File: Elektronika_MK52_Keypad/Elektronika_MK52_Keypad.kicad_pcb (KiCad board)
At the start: 2 copper layers, 33 parts, among them J1 Keypad PCB, SW1 F, SW10 ШГ←, SW11 Х←П, SW12 4, SW13 5, SW14 6, SW15 +, SW16 *, SW17 ↓↑, SW18 B/O, SW19 БП, SW2 ШГ→, SW20 1, SW21 2, SW22 3, SW23 ↔, SW24 В↑, SW25 A↑, SW26 С/П, SW27 ПП, SW28 0, SW29 ., SW3 П→Х, SW30 /-/, SW31 ВП, SW32 СХ, SW4 7, SW5 8, SW6 9, SW7 -, SW8 ÷, SW9 K

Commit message: Adjusted PCB thickness 1.6mm -> 1.0mm
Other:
- board outline added: 104 x 52.5 mm
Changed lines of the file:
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@@
 	(generator_version "9.0")
 	(general
-		(thickness 1.6)
+		(thickness 1)
 		(legacy_teardrops no)
 	)
@@
 	)
 	(setup
+		(stackup
+			(layer "F.SilkS"
+				(type "Top Silk Screen")
+			)
+			(layer "F.Paste"
+				(type "Top Solder Paste")
+			)
+			(layer "F.Mask"
+				(type "Top Solder Mask")
+				(thickness 0.01)
+			)
+			(layer "F.Cu"
+				(type "copper")
+				(thickness 0.035)
+			)
+			(layer "dielectric 1"
+				(type "core")
+				(thickness 0.91)
+				(material "FR4")
+				(epsilon_r 4.5)
+				(loss_tangent 0.02)
+			)
+			(layer "B.Cu"
+				(type "copper")
+				(thickness 0.035)
+			)
+			(layer "B.Mask"
+				(type "Bottom Solder Mask")
+				(thickness 0.01)
+			)
+			(layer "B.Paste"
+				(type "Bottom Solder Paste")
+			)
+			(layer "B.SilkS"
+				(type "Bottom Silk Screen")
+			)
+			(copper_finish "None")
+			(dielectric_constraints no)
+		)
 		(pad_to_mask_clearance 0)
 		(allow_soldermask_bridges_in_footprints no)
@@
 		(layer "Dwgs.User")
 	)
+	(gr_rect
+		(start 67 44)
+		(end 171 96.5)
+		(stroke
+			(width 0.05)
+			(type default)
+		)
+		(fill no)
+		(layer "Edge.Cuts")
+	)
 	(gr_text "WORK IN PROGRESS"

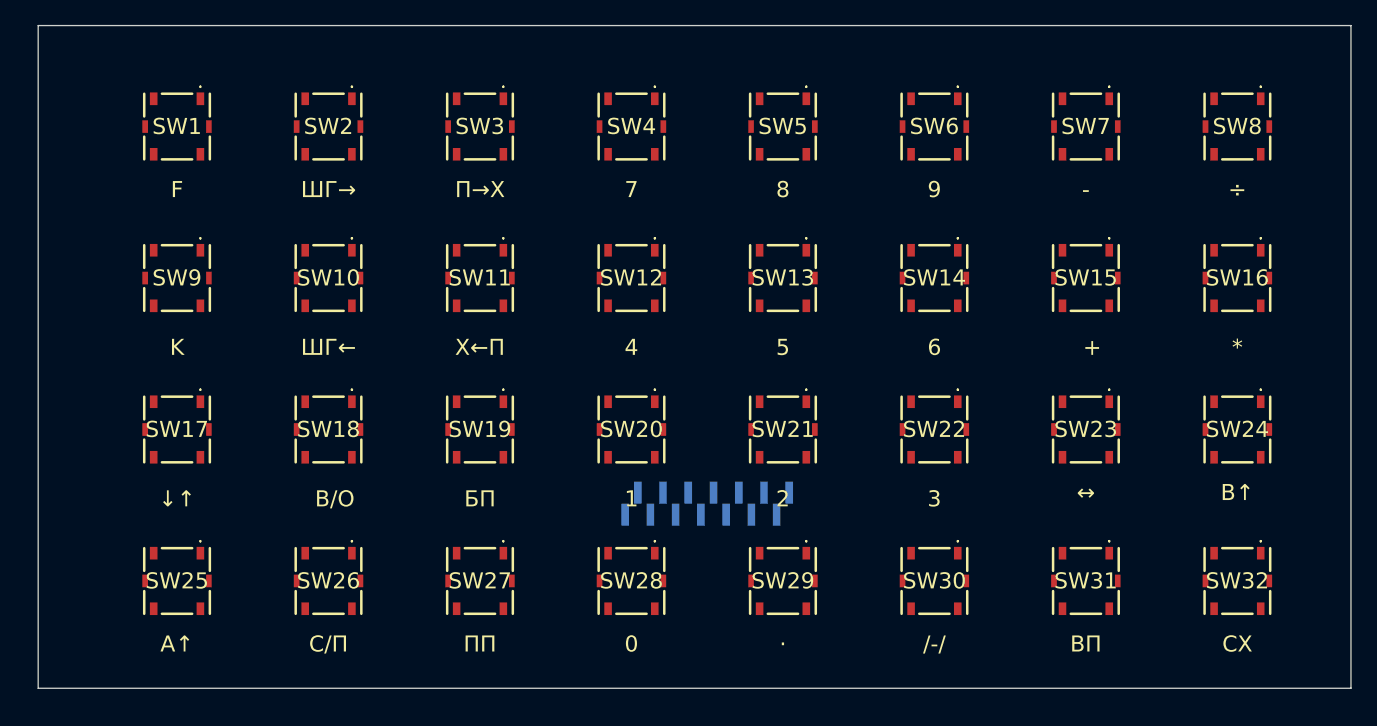
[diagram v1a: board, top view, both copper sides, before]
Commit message: Created PCB outline
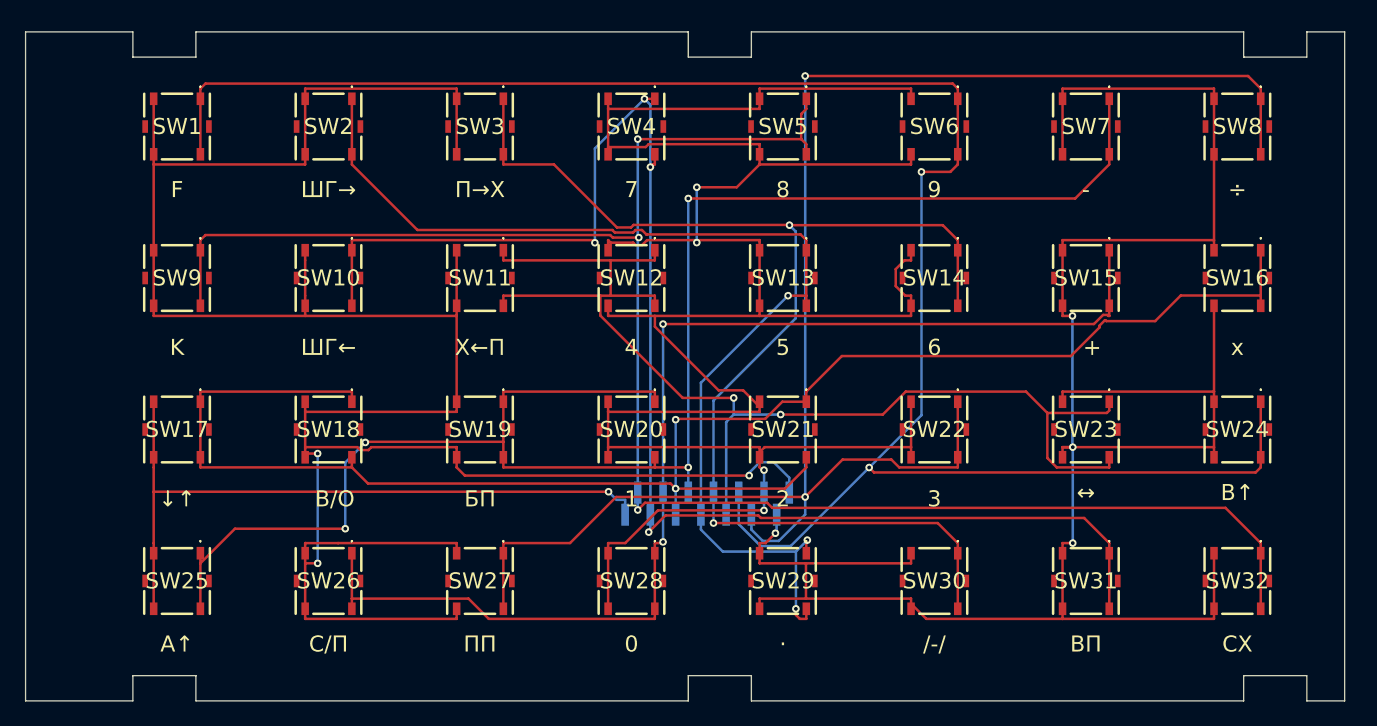
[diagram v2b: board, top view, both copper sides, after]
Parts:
- SW16: value * -> x
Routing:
- net /ROW 1: track 0.00 -> 199.7 mm, vias 0 -> 4
- net /ROW 0: track 0.00 -> 195.8 mm, vias 0 -> 3
- net /ROW 2: track 0.00 -> 175.6 mm, vias 0 -> 4
- net /COL 0: track 0.00 -> 152.5 mm, vias 0 -> 2
- net /COL 3: track 0.00 -> 143.4 mm, vias 0 -> 3
- net /COL 6: track 0.00 -> 132.7 mm, vias 0 -> 2
- net /COL 7: track 0.00 -> 132.7 mm, vias 0 -> 4
- net /COL 8: track 0.00 -> 132.5 mm, vias 0 -> 2
- net /COL 4: track 0.00 -> 117.3 mm, vias 0 -> 4
- net /COL 2: track 0.00 -> 100.8 mm, vias 0 -> 2
- net /COL 5: track 0.00 -> 95.9 mm, vias 0 -> 2
- net /COL 9: track 0.00 -> 93.9 mm, vias 0 -> 2
- net /COL 1: track 0.00 -> 89.3 mm, vias 0 -> 3
- net /ROW 3: track 0.00 -> 55.2 mm, vias 0 -> 1
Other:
- board size 104 x 52.5 mm -> 104.5 x 53 mm

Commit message: initial PCB routing
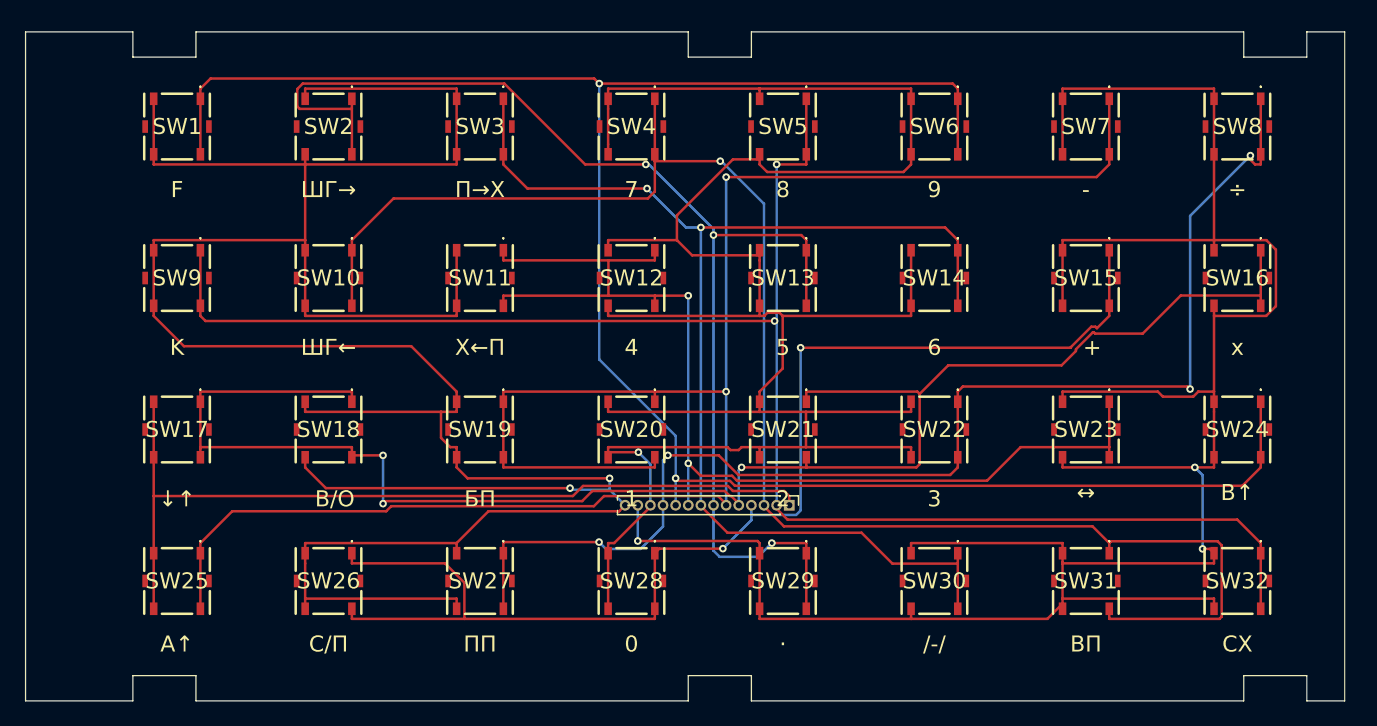
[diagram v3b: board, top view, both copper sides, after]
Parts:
- J1: footprint Connector_PinHeader_1.00mm:PinHeader_1x14_P1.00mm_Vertical_SMD_Pin1Right -> Connector_PinHeader_1.00mm:PinHeader_1x14_P1.00mm_Vertical; moved to F.Cu
- moved J1 6.50 mm to (126.5, 82.0)
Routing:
- net /ROW 0: track 195.8 -> 228.3 mm, vias 3 -> 2
- net /COL 8: track 132.5 -> 100.1 mm, vias 2 -> 4
- net /ROW 2: track 175.6 -> 196.1 mm, vias 4 -> 3
- net /COL 7: track 132.7 -> 148.0 mm, vias 4 -> 2
- net /ROW 3: track 55.2 -> 68.1 mm, vias 1 -> 0
- net /COL 3: track 143.4 -> 130.5 mm, vias 3 -> 2
- net /ROW 1: track 199.7 -> 188.6 mm, vias 4 -> 1
- net /COL 1: track 89.3 -> 99.5 mm
- net /COL 4: track 117.3 -> 126.1 mm, vias 4 -> 1
- net /COL 5: track 95.9 -> 88.7 mm
- net /COL 9: track 93.9 -> 100.9 mm
- net /COL 0: track 152.5 -> 159.4 mm
- net /COL 2: track 100.8 -> 97.6 mm
- net /COL 6: track 132.7 -> 134.6 mm, vias 2 -> 3

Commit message: Adjusted PCB dimensions (thanks Alex!)
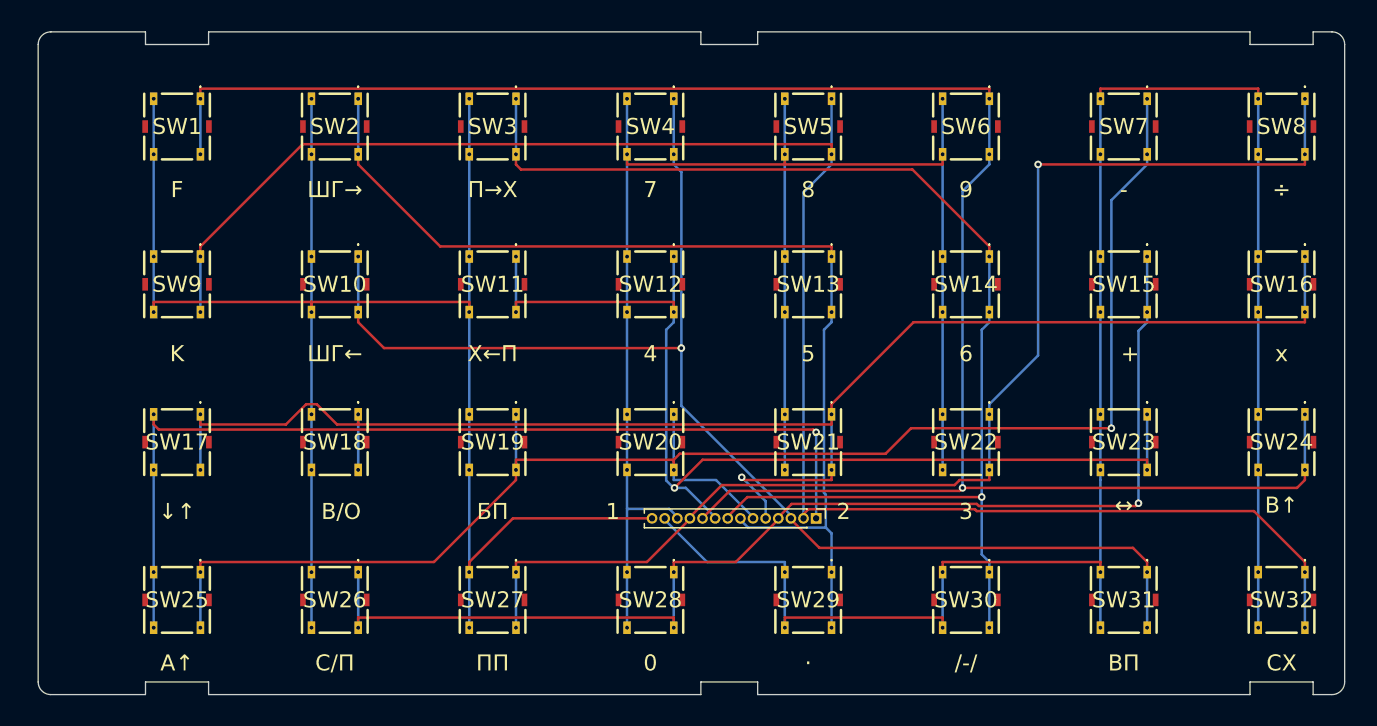
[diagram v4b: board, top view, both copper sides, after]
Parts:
- moved SW32 3.81 mm to (165.5, 89.5)
- moved SW24 3.64 mm to (165.5, 77.0)
- moved SW16 3.54 mm to (165.5, 64.5)
- moved SW8 3.50 mm to (165.5, 52.0)
- moved SW31 3.35 mm to (153.0, 89.5)
- moved SW23 3.16 mm to (153.0, 77.0)
- moved SW15 3.04 mm to (153.0, 64.5)
- moved SW7 3.00 mm to (153.0, 52.0)
- moved SW30 2.92 mm to (140.5, 89.5)
- moved SW22 2.69 mm to (140.5, 77.0)
- moved SW14 2.55 mm to (140.5, 64.5)
- moved SW29 2.50 mm to (128.0, 89.5)
- moved SW6 2.50 mm to (140.5, 52.0)
- moved J1 2.37 mm to (128.6, 83.0)
- moved SW21 2.24 mm to (128.0, 77.0)
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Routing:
- net /ROW 0: track 228.3 -> 144.8 mm, vias 2 -> 0
- net /ROW 1: track 188.6 -> 132.5 mm, vias 1 -> 0
- net /ROW 2: track 196.1 -> 146.7 mm, vias 3 -> 0
- net /COL 4: track 126.1 -> 103.6 mm
- net /COL 7: track 148.0 -> 128.0 mm, vias 2 -> 1
- net /COL 1: track 99.5 -> 83.2 mm, vias 3 -> 0
- net /COL 3: track 130.5 -> 140.7 mm, vias 2 -> 0
- net /COL 6: track 134.6 -> 125.2 mm, vias 3 -> 1
- net /ROW 3: track 68.1 -> 77.3 mm, vias 0 -> 1
- net /COL 9: track 100.9 -> 95.0 mm, vias 2 -> 1
- net /COL 0: track 159.4 -> 154.4 mm, vias 2 -> 1
- net /COL 5: track 88.7 -> 85.2 mm, vias 2 -> 1
- net /COL 8: track 100.1 -> 98.4 mm, vias 4 -> 1
- net /COL 2: track 97.6 -> 97.0 mm, vias 2 -> 1
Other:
- board size 104.5 x 53 mm -> 103.5 x 52.5 mm

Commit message: Revised PCB layout
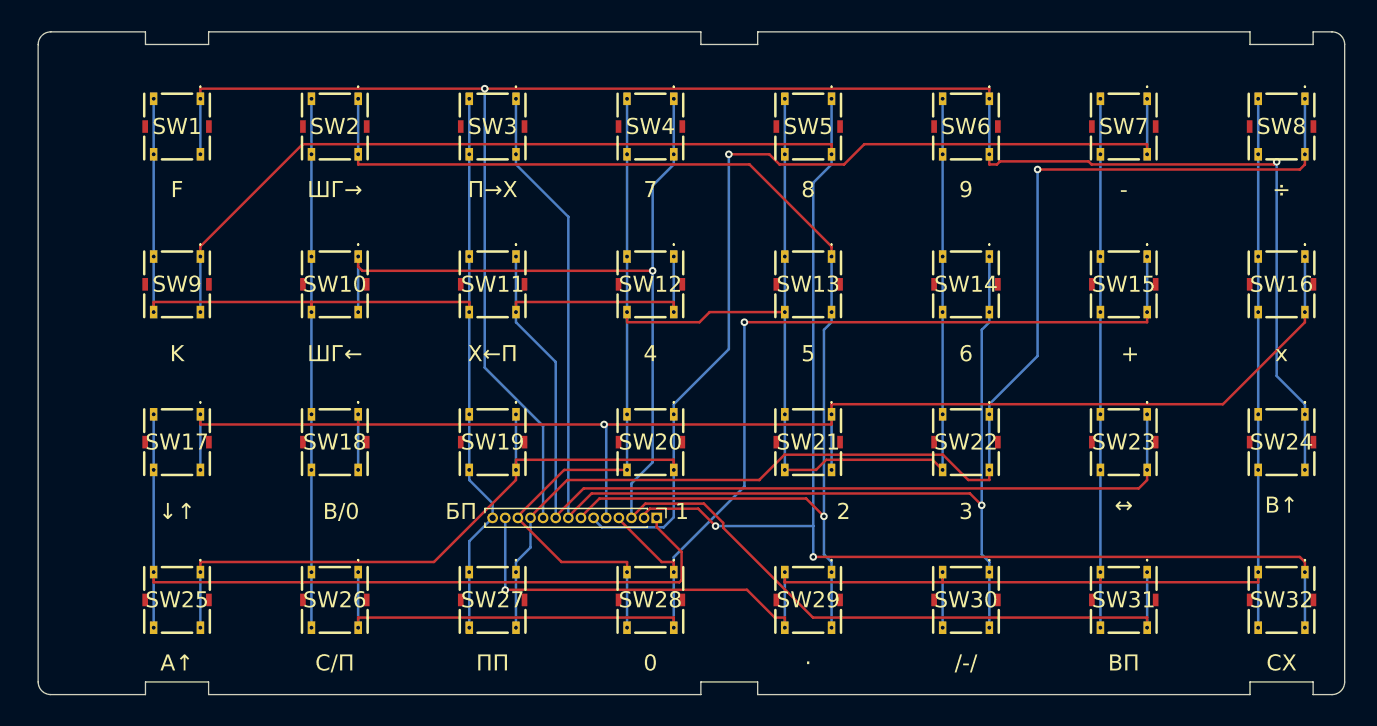
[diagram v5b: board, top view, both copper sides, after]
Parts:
- SW18: value B/O -> B/0
- moved J1 12.6 mm to (116.0, 83.0)
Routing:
- net /ROW 2: track 146.7 -> 162.9 mm, vias 0 -> 1
- net /ROW 0: track 144.8 -> 129.6 mm
- net /COL 3: track 140.7 -> 155.0 mm, vias 0 -> 2
- net /COL 1: track 83.2 -> 96.6 mm, vias 0 -> 1
- net /ROW 3: track 77.3 -> 65.3 mm, vias 1 -> 0
- net /COL 4: track 103.6 -> 113.8 mm
- net /COL 5: track 85.2 -> 93.9 mm, vias 1 -> 0
- net /ROW 1: track 132.5 -> 140.6 mm
- net /COL 9: track 95.0 -> 101.3 mm
- net /COL 6: track 125.2 -> 119.3 mm
- net /COL 0: track 154.4 -> 158.0 mm, vias 1 -> 2
- net /COL 8: track 98.4 -> 101.2 mm
- net /COL 2: track 97.0 -> 98.8 mm
- net /COL 7: track 128.0 -> 129.1 mm
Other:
- board text added: "1"
- board text added: "14"
- board text added: "Сменная Клавиатура Для Электроника МК-52 Replacement Keypad For Elektronika MK-52 Brett Hallen, Dec 2025 www.youtube.com/@Brfff"
